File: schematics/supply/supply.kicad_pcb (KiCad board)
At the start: 4 copper layers, 224 x 175 mm, 307 parts, among them J1 Conn_01x02_Pin, J11 Conn_01x04_Pin, J13 USBASP, J14 USBASP, J15 Conn_01x06_Pin, J17 banana jack + fuse 15A, J18 banana jack + fuse 15A, J19 Conn_02x04_Odd_Even, J2 Conn_01x02_Pin, J20 jst xh angle, J21 jst xh angle, J3 Conn_01x01_Pin, J4 Conn_01x01_Pin, J5 CW2B-10A-T, J6 USB_A, J7 USB_A, J8 USB_A, J9 Conn_01x04_Pin, K1 SRD-12VDC-SL-C, M1 Fan, Q1 STP13NK60Z, Q10 IRLML0030, Q11 IRLML0030, Q12 IRLML0030, Q13 IRLML5203, Q14 IRLML5203, Q2 IRLML5203, Q3 40N06, Q4 STP13NK60Z, Q5 STP13NK60Z, Q6 IRLML0030, Q7 IRLML5203, Q8 IRLML5203, Q9 IRLML0030, SW3 SW_Push, U1 ICE2PCS01, U10 IRS2153S, U11 LM158DR, U12 IP2163, U13 LM158DR, U14 TL432DBZ, U15 LM158DR, U16 LM1085-3.3, U17 ATmega328-A, U18 ATtiny1616-M, U2 TL331, U20 LM158DR, U21 EL817, U22 IRS2153S, U23 TL331, U24 INA169, U25 INA3221, U3 R7731, U4 EL817, U5 TL432DBZ, U6 INA3221, U7 EL817, U8 MC34063AD, U9 L78L33ACUTR, X1 HC-49U, 16MHz, X2 CSX-750FCC, 16MHz, Y1 B32022A3223M000

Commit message: One board settings changed from 4-layers to 2-layers to reduce it's price
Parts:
- removed JP1: PFC_VCC_OK#, Jumper:SolderJumper-2_P1.3mm_Open_TrianglePad1.0x1.5mm
- added JP7: PFC_VCC_OK#, TestPoint:TestPoint_2Pads_Pitch2.54mm_Drill0.8mm, F.Cu at (278.2, 142.5)
- added R20: 1K2, Resistor_SMD:R_0805_2012Metric, B.Cu at (131.2, 181.5)
- C20: value 0.1 uF -> 100 nF
- D14, D17, D9: value BL-L109EGW -> red/green, common cathode, F3
- R15: value 4K5 -> 4K7
- R5: value 65K -> 62K
- moved C4 22.5 mm to (291.9, 136.3)
- moved L1 22.5 mm to (295.4, 110.0)
- moved R7 22.5 mm to (291.7, 142.1)
- moved C1 22.5 mm to (229.2, 109.6)
- moved CLR1 22.5 mm to (243.9, 91.5)
- moved CLR2 22.5 mm to (250.0, 155.1)
- moved CP5 22.5 mm to (229.9, 137.7)
- moved D1 22.5 mm to (236.1, 94.0)
- moved Q2 22.5 mm to (278.2, 128.6)
- moved R17 22.5 mm to (278.0, 132.1)
- moved RP12 22.5 mm to (265.8, 118.7)
- moved RP13 22.5 mm to (241.7, 159.1)
- moved RP16 22.5 mm to (253.9, 162.6)
- moved TP1 22.5 mm to (225.9, 124.6)
- moved C10 22.5 mm to (285.1, 135.8)
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- renumbered R20 to R21, R21 to R22, R22 to R23, R23 to R24, R24 to R25, R25 to R26, R26 to R27, R27 to R28, R28 to R29, R29 to R30, R30 to R31, R31 to R32, R32 to R33, R33 to R34, R34 to R35, R35 to R36, R36 to R37, R37 to R38, R38 to R39, R39 to R40, R40 to R41, R41 to R42, R42 to R43, R43 to R44, R44 to R45, R45 to R46, R46 to R47, R47 to R48, R48 to R49, R49 to R50, R50 to R51, R51 to R52, R52 to R53, R53 to R54, R54 to R55, R55 to R56, R56 to R57, R57 to R58, R58 to R59, R59 to R60, R60 to R61, R61 to R62, R62 to R63, R63 to R64, R64 to R65, R65 to R66, R66 to R67, R67 to R68, R68 to R69, R69 to R70, R70 to R71, R71 to R72, R72 to R73, R73 to R74, R74 to R75, R75 to R76, R76 to R77, R77 to R78, R78 to R79
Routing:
- net /Input power with filter/HV_GND: track 612.4 -> 560.1 mm
- net /Input power with filter/PFC_VCC: track 114.5 -> 121.5 mm, vias 3 -> 2
- net /Internal 5V & out usb/FEEDBACK: track 21.9 -> 25.4 mm
- net /Input power with filter/VOUT_PRE_PFC: track 96.5 -> 99.7 mm
- net Net-(DP1-K): track 160.2 -> 163.0 mm
- net Net-(R19-Pad1): track 9.20 -> 11.2 mm
- net /Input power with filter/PFC_OK#: track 31.9 -> 30.4 mm, vias 1 -> 0
- net /Internal 5V & out usb/+5V_OUT: track 314.2 -> 312.9 mm
- net /Input power with filter/VOUT_PRE_GND: track 94.6 -> 94.0 mm
- net Net-(JP7-B): track 12.8 -> 12.9 mm, vias 1 -> 0
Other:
- board size 224 x 175 mm -> 246.4 x 175.2 mm
- board text added: "G"
- board text added: "R"

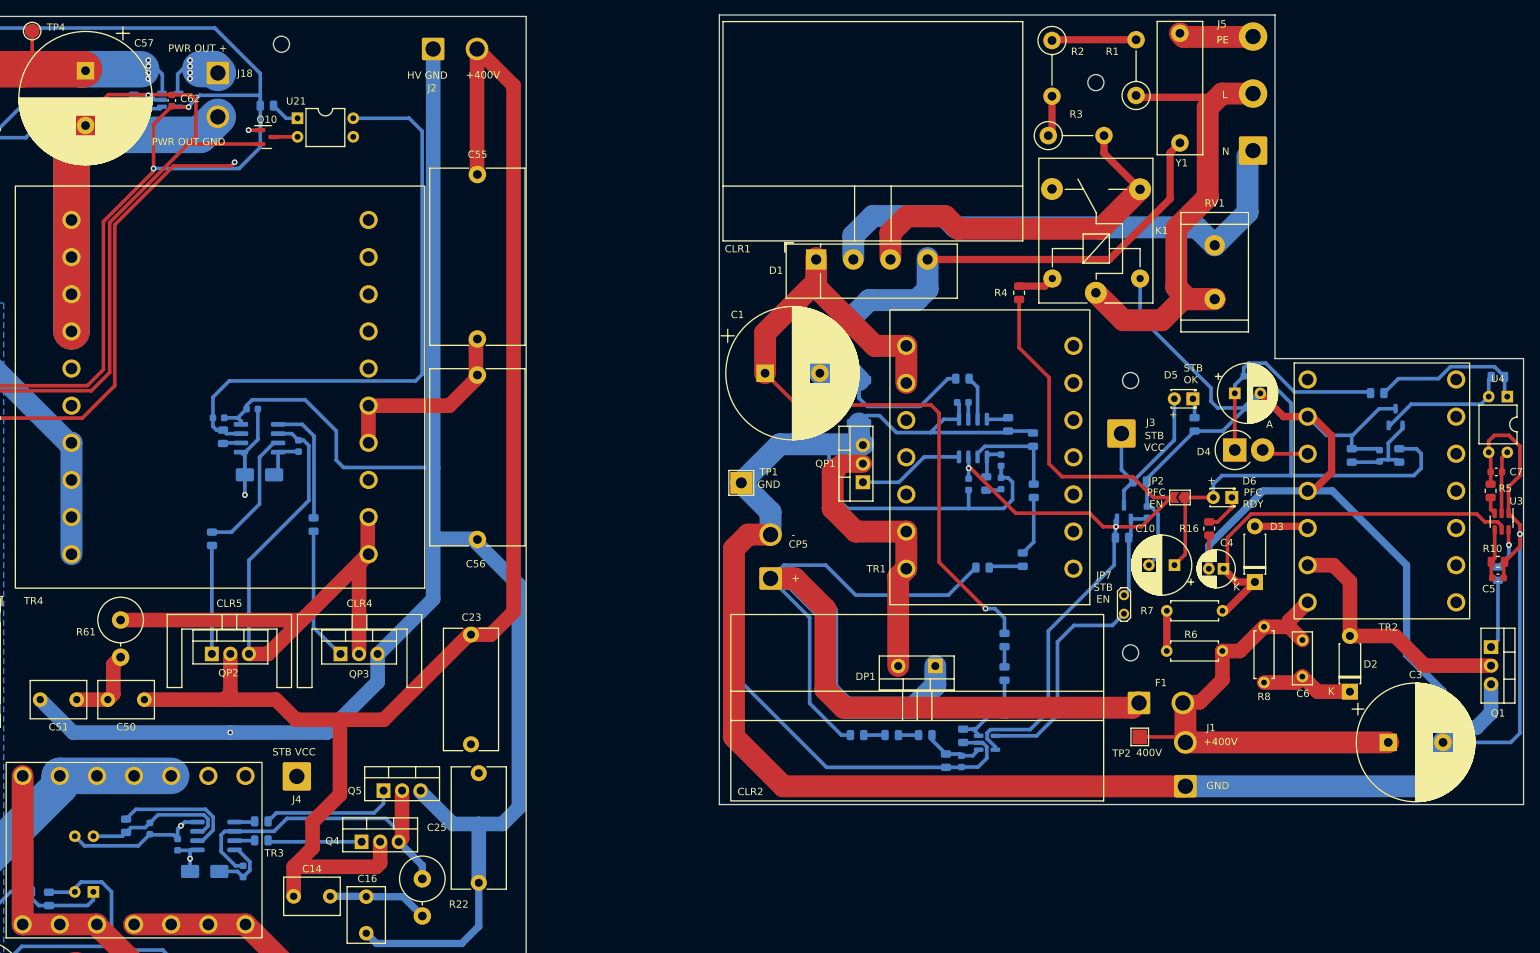
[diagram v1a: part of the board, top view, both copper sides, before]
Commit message: Project splited to 2 sub-projects - I want to reduce board production price
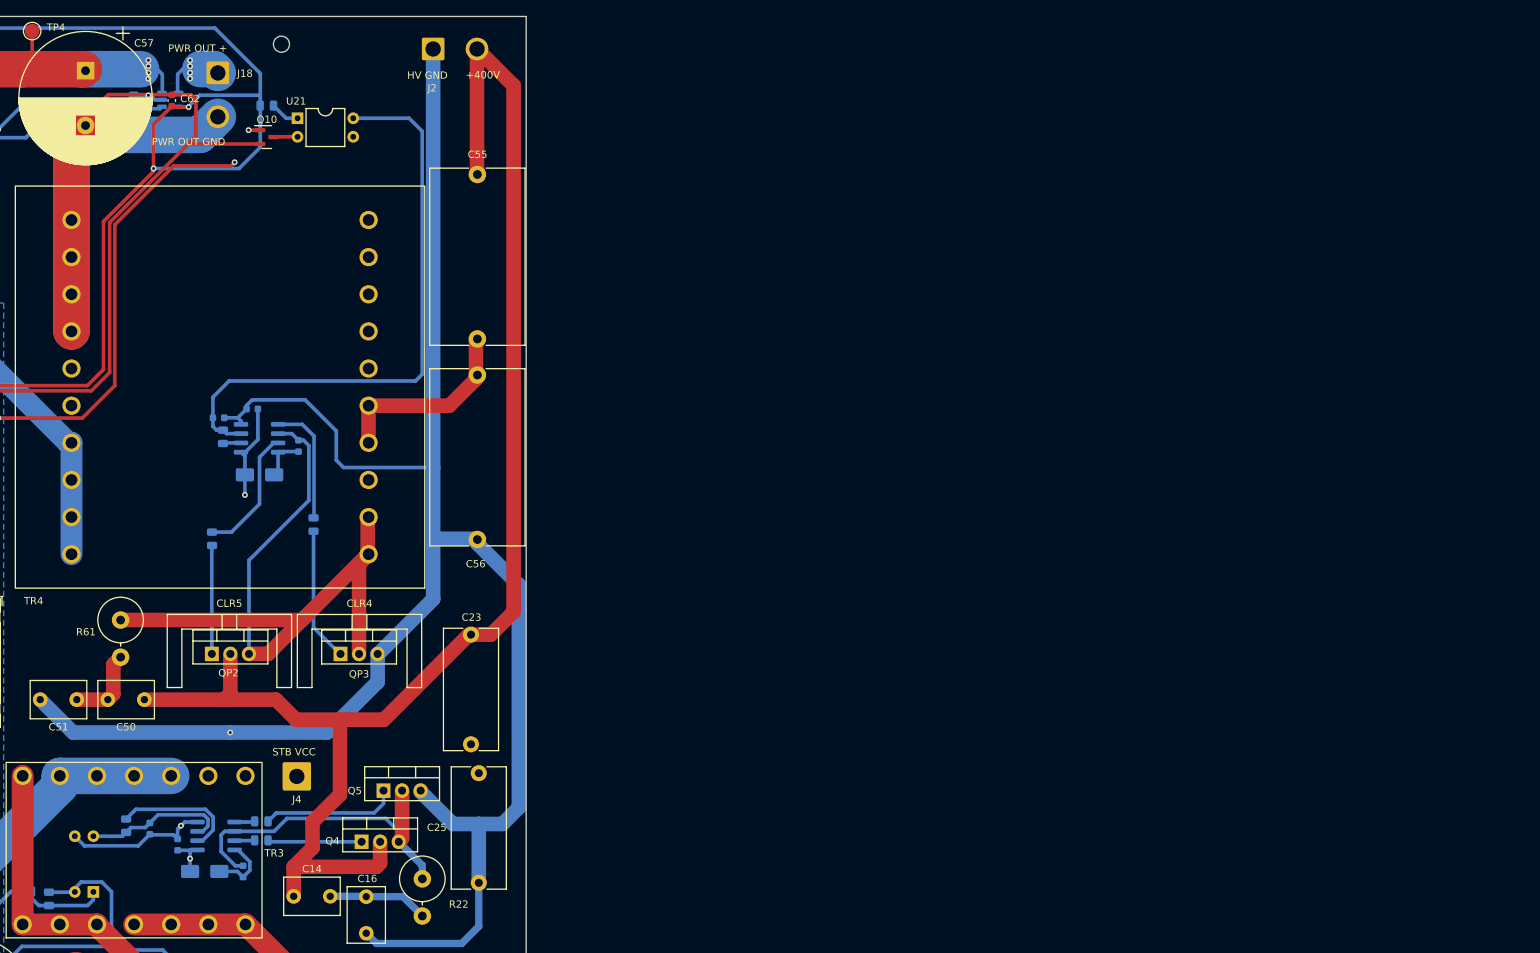
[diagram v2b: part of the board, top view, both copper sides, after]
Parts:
- removed C1: 100 uF@350V, Capacitor_THT:CP_Radial_D18.0mm_P7.50mm
- removed C10, C8: 220 uF@35V, Capacitor_THT:CP_Radial_D8.0mm_P3.50mm
- removed C11, CP1, CP3: 100 nF, Capacitor_SMD:C_0603_1608Metric
- removed C2, CP2, CP4: 1 uF, Capacitor_SMD:C_0603_1608Metric
- removed C3: 47 uF@450V, Capacitor_THT:CP_Radial_D16.0mm_P7.50mm
- removed C4: 22 uF@50V, Capacitor_THT:CP_Radial_D5.0mm_P2.00mm
- removed C5, C7, C9: 10 nF, Capacitor_SMD:C_0603_1608Metric
- removed C6: JYC3D101KBY, Capacitor_THT:C_Disc_D7.0mm_W2.5mm_P5.00mm
- removed CLR1: HS 184-30@30х41х30mm, Library:HS-184-30
- removed CLR2: HS 216-30@30х51х25.5mm, Library:HS 216-30
- removed CP5: 3300 uF@450V, Connector_Wire:SolderWire-1.5sqmm_1x02_P6mm_D1.7mm_OD3mm
- removed D1: KBU1010, Diode_THT:Diode_Bridge_Vishay_KBU
- removed D2, D3: FR107, Diode_THT:D_DO-41_SOD81_P7.62mm_Horizontal
- removed D4: FR303, Diode_THT:D_DO-201AD_P3.81mm_Vertical_AnodeUp
- removed D5, D6: L-2060YD, LED_THT:LED_D1.8mm_W3.3mm_H2.4mm
- removed DP1: STTH8S06D, Package_TO_SOT_THT:TO-220-2_Vertical
- removed F1: C10G4 with fuseholder, Connector_Wire:SolderWire-1.5sqmm_1x02_P6mm_D1.7mm_OD3mm
- removed H10, H8, H9: MountingHole, MountingHole:MountingHole_2.2mm_M2
- removed J1: Conn_01x02_Pin, Connector_Wire:SolderWire-1.5sqmm_1x02_P6mm_D1.7mm_OD3mm
- removed J3: Conn_01x01_Pin, Connector_Wire:SolderWire-1.5sqmm_1x01_D1.7mm_OD3.9mm
- removed J5: CW2B-10A-T, Connector_Wire:SolderWire-1.5sqmm_1x03_P7.8mm_D1.7mm_OD3.9mm
- removed JP2: PFC Enable, Jumper:SolderJumper-2_P1.3mm_Open_TrianglePad1.0x1.5mm
- removed JP7: PFC_VCC_OK#, TestPoint:TestPoint_2Pads_Pitch2.54mm_Drill0.8mm
- removed K1: SRD-12VDC-SL-C, Relay_THT:Relay_SPDT_SANYOU_SRD_Series_Form_C
- removed L1: BLM18EG221SN1D, Inductor_SMD:L_0603_1608Metric
- removed Q1, QP1: STP13NK60Z, Package_TO_SOT_THT:TO-220-3_Vertical
- removed Q2: IRLML5203, Package_TO_SOT_SMD:SOT-23
- removed R1, R2, R3: JNR13S500L, Resistor_THT:R_Axial_DIN0411_L9.9mm_D3.6mm_P7.62mm_Vertical
- removed R10, R17, RP3: 10K, Resistor_SMD:R_0805_2012Metric
- removed R11, R12, R16: 1K, Resistor_SMD:R_0805_2012Metric
- removed R13: 1K2, Resistor_SMD:R_0805_2012Metric
- removed R14, RP1: 20K, Resistor_SMD:R_0805_2012Metric
- removed R15: 4K7, Resistor_SMD:R_0805_2012Metric
- removed R18: 200K, Resistor_SMD:R_0805_2012Metric
- removed R4: 50, Resistor_SMD:R_0805_2012Metric
- removed R5: 62K, Resistor_SMD:R_0805_2012Metric
- removed R6, R7: 1M, Resistor_THT:R_Axial_DIN0207_L6.3mm_D2.5mm_P7.62mm_Horizontal
- removed R8: 305K, Resistor_THT:R_Axial_DIN0207_L6.3mm_D2.5mm_P7.62mm_Horizontal
- removed R9: 33, Resistor_SMD:R_0805_2012Metric
- removed RP10, RP11, RP13, RP14, RP15, RP5, RP6, RP7, RP9: 750K, Resistor_SMD:R_0805_2012Metric
- removed RP12: 17K, Resistor_SMD:R_0805_2012Metric
- removed RP16: 60K, Resistor_SMD:R_0805_2012Metric
- removed RP2: 0.01, Resistor_SMD:R_2512_6332Metric
- removed RP4: 220, Resistor_SMD:R_0805_2012Metric
- removed RP8: 70K, Resistor_SMD:R_0805_2012Metric
- removed RV1: FNR-14K431, Resistor_THT:R_Radial_Power_L16.1mm_W9.0mm_P7.37mm
- removed TP1: HV GND, TestPoint:TestPoint_THTPad_3.0x3.0mm_Drill1.5mm
- removed TP2: 400V, TestPoint:TestPoint_Pad_2.0x2.0mm
- removed TR1: ETD 34/17/11@N87@s=5mm N25@1mm*2, Library:ETD34_7x7_vertical
- removed TR2: ETD 29/16/10@N87@s=0.2mm N56/13/9@0.5mm, Library:ETD29_7x7_vertical
- removed U1: ICE2PCS01, Package_SO:SO-8_3.9x4.9mm_P1.27mm
- removed U2: TL331, Package_TO_SOT_SMD:SOT-23-5
- removed U3: R7731, Package_TO_SOT_SMD:SOT-23-6
- removed U4: EL817, Package_DIP:DIP-4_W7.62mm
- removed U5: TL432DBZ, Package_TO_SOT_SMD:SOT-23-3
- removed Y1: B32022A3223M000, Capacitor_THT:C_Rect_L18.0mm_W6.0mm_P15.00mm_FKS3_FKP3
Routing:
- net /Input power with filter/HV_GND: track 560.1 -> 0.00 mm, vias 1 -> 0
- net Net-(DP1-K): track 163.0 -> 0.00 mm
- net /Input power with filter/PFC_VCC: track 121.5 -> 0.00 mm, vias 2 -> 0
- net /Input power with filter/VOUT_PRE_PFC: track 99.7 -> 0.00 mm, vias 1 -> 0
- net /Input power with filter/VOUT_PRE_GND: track 94.0 -> 0.00 mm
- net /Input power with filter/STARTUP_PROTECT_IN: track 73.5 -> 0.00 mm
- net Net-(J5-Pin_1): track 70.4 -> 0.00 mm
- net Net-(D6-A): track 66.5 -> 0.00 mm
- net /Input power with filter/OUT_400V: track 65.8 -> 0.00 mm
- net Net-(D3-K): track 54.9 -> 0.00 mm
- net /Input power with filter/STARTUP_PROTECT_OUT: track 50.9 -> 0.00 mm
- net Net-(DP1-A): track 39.8 -> 0.00 mm
- net Net-(D2-A): track 35.1 -> 0.00 mm
- net Net-(D4-K): track 30.8 -> 0.00 mm
- net /Input power with filter/PFC_OK#: track 30.4 -> 0.00 mm
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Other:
- board size 246.4 x 175.2 mm -> 110 x 175 mm
- board text removed: "400V"
- board text removed: "Capacitor 3300uF@450V"
- board text removed: "L"
- board text removed: "N"
- board text removed: "PE"
- board text removed: "PFC EN"
- board text removed: "PFC RDY"
- board text removed: "STB EN"
- board text removed: "STB OK"
- board text removed: "Supply board#1 v1.0"

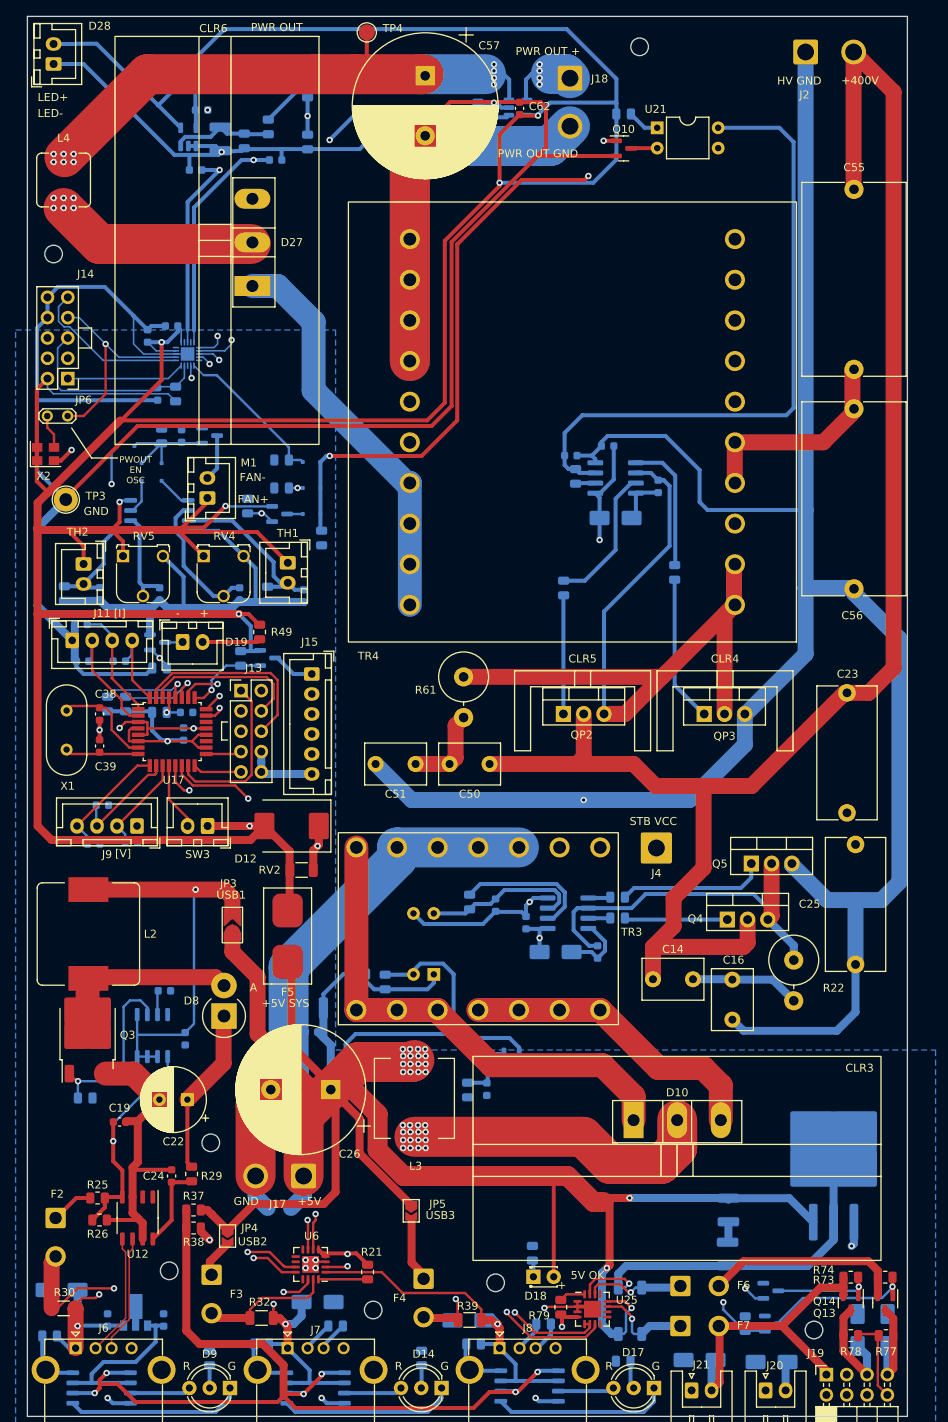
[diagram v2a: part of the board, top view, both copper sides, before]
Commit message: UV board size changed to 100x100 to reduce production price
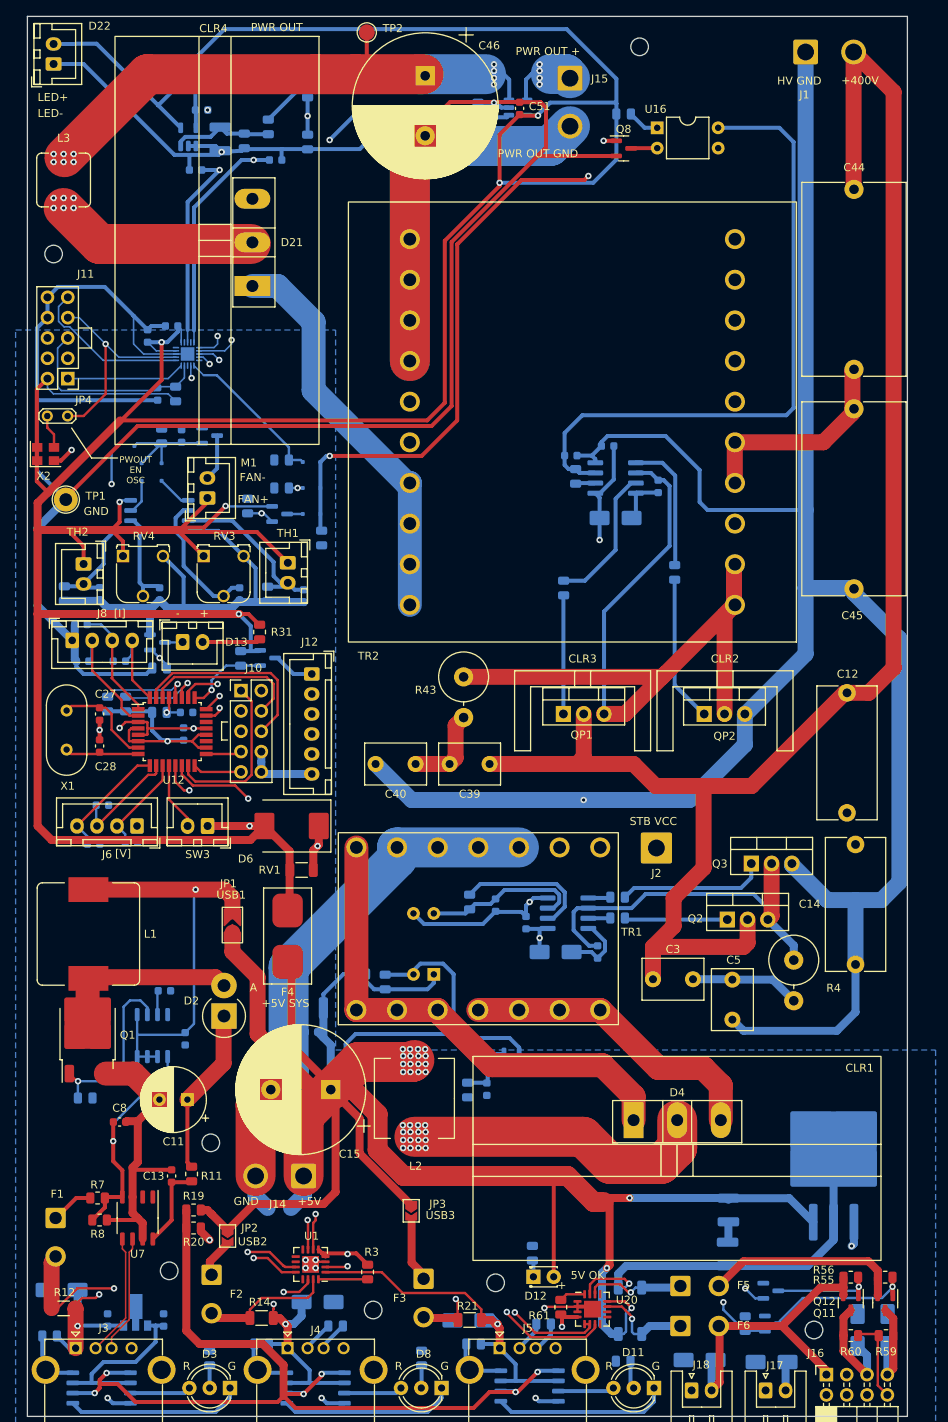
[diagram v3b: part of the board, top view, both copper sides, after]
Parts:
- renumbered C12 to C1, C21 to C10, C22 to C11, C23 to C12, C24 to C13, C25 to C14, C26 to C15, C27 to C16, C28 to C17, C29 to C18, C30 to C19, C13 to C2, C31 to C20, C32 to C21, C33 to C22, C34 to C23, C35 to C24, C36 to C25, C37 to C26, C38 to C27, C39 to C28, C40 to C29, C14 to C3, C41 to C30, C42 to C31, C43 to C32, C44 to C33, C45 to C34, C46 to C35, C47 to C36, C48 to C37, C49 to C38, C50 to C39, C15 to C4, C51 to C40, C52 to C41, C53 to C42, C54 to C43, C55 to C44, C56 to C45, C57 to C46, C58 to C47, C59 to C48, C60 to C49, C16 to C5, C61 to C50, C62 to C51, C17 to C6, C18 to C7, C19 to C8, C20 to C9, CLR3 to CLR1, CLR4 to CLR2, CLR5 to CLR3, CLR6 to CLR4, D7 to D1, D16 to D10, D17 to D11, D18 to D12, D19 to D13, D20 to D14, D21 to D15, D22 to D16, D23 to D17, D24 to D18, D25 to D19, D8 to D2, D26 to D20, D27 to D21, D28 to D22, D29 to D23, D30 to D24, D31 to D25, D32 to D26, D9 to D3, D10 to D4, D11 to D5, D12 to D6, D13 to D7, D14 to D8, D15 to D9, F2 to F1, F3 to F2, F4 to F3, F5 to F4, F6 to F5, F7 to F6, J2 to J1, J13 to J10, J14 to J11, J15 to J12, J17 to J14, J18 to J15, J19 to J16, J20 to J17, J21 to J18, J4 to J2, J6 to J3, J7 to J4, J8 to J5, J9 to J6, J11 to J8, JP3 to JP1, JP4 to JP2, JP5 to JP3, JP6 to JP4, L2 to L1, L3 to L2, L4 to L3, Q3 to Q1, Q12 to Q10, Q13 to Q11, Q14 to Q12, Q4 to Q2, Q5 to Q3, Q6 to Q4, Q7 to Q5, Q8 to Q6, Q9 to Q7, Q10 to Q8, Q11 to Q9, QP2 to QP1, QP3 to QP2, R19 to R1, R28 to R10, R29 to R11, R30 to R12, R31 to R13, R32 to R14, R33 to R15, R34 to R16, R35 to R17, R36 to R18, R37 to R19, R20 to R2, R38 to R20, R39 to R21, R40 to R22, R41 to R23, R42 to R24, R43 to R25, R44 to R26, R45 to R27, R46 to R28, R47 to R29, R21 to R3, R48 to R30, R49 to R31, R50 to R32, R51 to R33, R52 to R34, R53 to R35, R54 to R36, R55 to R37, R56 to R38, R57 to R39, R22 to R4, R58 to R40, R59 to R41, R60 to R42, R61 to R43, R62 to R44, R63 to R45, R64 to R46, R65 to R47, R66 to R48, R67 to R49, R23 to R5, R68 to R50, R69 to R51, R70 to R52, R71 to R53, R72 to R54, R73 to R55, R74 to R56, R75 to R57, R76 to R58, R77 to R59, R24 to R6, R78 to R60, R79 to R61, R25 to R7, R26 to R8, R27 to R9, RV2 to RV1, RV3 to RV2, RV4 to RV3, RV5 to RV4, TP3 to TP1, TP4 to TP2, TR3 to TR1, TR4 to TR2, U6 to U1, U15 to U10, U16 to U11, U17 to U12, U18 to U13, U20 to U15, U21 to U16, U22 to U17, U23 to U18, U24 to U19, U7 to U2, U25 to U20, U8 to U3, U9 to U4, U10 to U5, U11 to U6, U12 to U7, U13 to U8, U14 to U9
